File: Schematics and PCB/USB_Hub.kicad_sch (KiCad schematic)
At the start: 95 parts, among them J6 UPSTREAM, J7 DOWNSTREAM_3, J8 DOWNSTREAM_1, J9 DOWNSTREAM_1, U16 TLV71311PDBVR, U17 TUSB8042A, U18 TPS2561, U19 TPS2561, U21 TLV70033DDCR, Y1 24MHz 20pF GND24

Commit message: Finished initial iteration of the Right layout
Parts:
- renumbered C101 to C195, C209 to C196, C195 to C197, C197 to C199, C208 to C202, C212 to C203, C200 to C204, C202 to C205, C203 to C207, C205 to C209, R102 to R100, R103 to R101, R104 to R102, R83 to R75, R82 to R76, R81 to R77, R80 to R78, R77 to R79, R78 to R80, R79 to R81, R84 to R82, R85 to R83, R87 to R85, R88 to R86, R89 to R87, R90 to R88, R91 to R89, R92 to R90, R93 to R91, R94 to R92, R95 to R93, R96 to R94, R97 to R95, R98 to R96, R99 to R97, R100 to R98, R101 to R99, U17 to U16, U18 to U17, U16 to U18, U21 to U19, U19 to U20

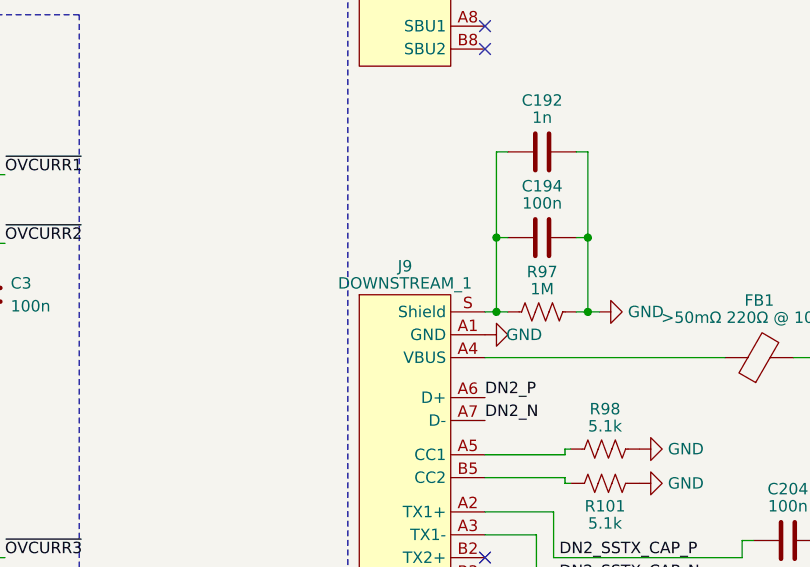
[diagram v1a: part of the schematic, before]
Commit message: Started USB hub layout and added footprints
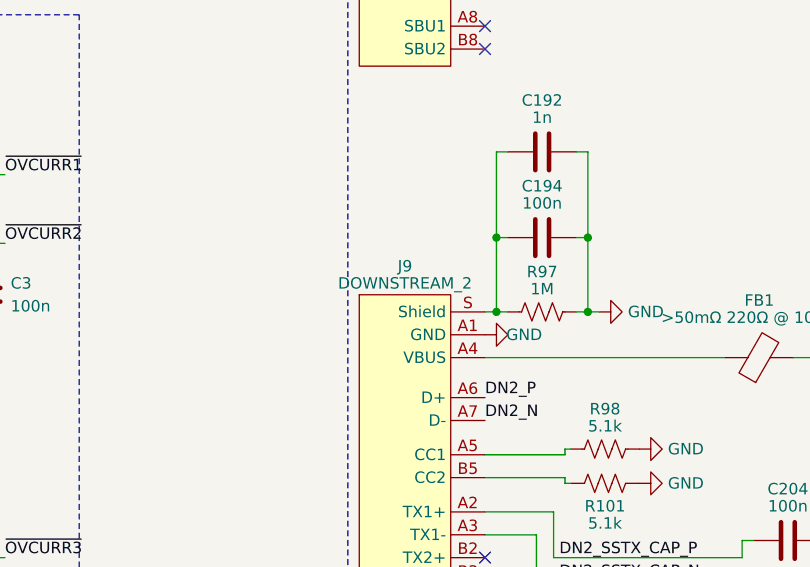
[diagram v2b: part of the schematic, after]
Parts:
- C160, C161, C163, C164, C167, C168, C169, C170, C171, C179, C180, C181, C190, C192, C194, C195, C196, C202, C203, C204, C205, C3, C4: footprint (none) -> Capacitor_SMD:C_0603_1608Metric
- C176, C189, C197, C199, C207, C209: footprint (none) -> Capacitor_Tantalum_SMD:CP_EIA-3216-18_Kemet-A
- FB1: footprint (none) -> Inductor_SMD:L_0805_2012Metric
- J6, J8: footprint (none) -> Connector_USB:USB_C_Receptacle_Amphenol_12401610E4-2A
- J7: footprint (none) -> Connector_USB:USB3_A_Molex_48393-001
- J9: value DOWNSTREAM_1 -> DOWNSTREAM_2; footprint (none) -> Connector_USB:USB_C_Receptacle_Amphenol_12401610E4-2A
- R100, R101, R102, R75, R76, R77, R78, R80, R81, R82, R83, R85, R86, R87, R88, R89, R92, R93, R94, R95, R96, R98, R99: footprint (none) -> Resistor_SMD:R_0603_1608Metric
- U16: footprint (none) -> Package_DFN_QFN:VQFN-64-1EP_9x9mm_P0.5mm_EP7.15x7.15mm
- Y1: footprint (none) -> Crystal:Crystal_SMD_3225-4Pin_3.2x2.5mm
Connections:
- net DN1_N: now also J8.B7 (D-)
- net DN2_N: now also J9.B7 (D-)
- net GND: now also J6.B1 (GND), J6.B12 (GND), J8.B1 (GND), J8.B12 (GND), J9.B1 (GND), J9.B12 (GND)
- net UP_N: now also J6.B7 (D-)
- net UP_VBUS: now also J6.B4 (VBUS), J6.B9 (VBUS)
- net at FB1.1, J9.A4 (VBUS), J9.A9 (VBUS): now also J9.B4 (VBUS), J9.B9 (VBUS)
- net at FB1.1, J8.A4 (VBUS), J8.A9 (VBUS): now also J8.B4 (VBUS), J8.B9 (VBUS)
